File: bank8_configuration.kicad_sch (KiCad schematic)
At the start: 19 parts, among them IC1 ECP5-BGA256, U7 W25Q32JVSS

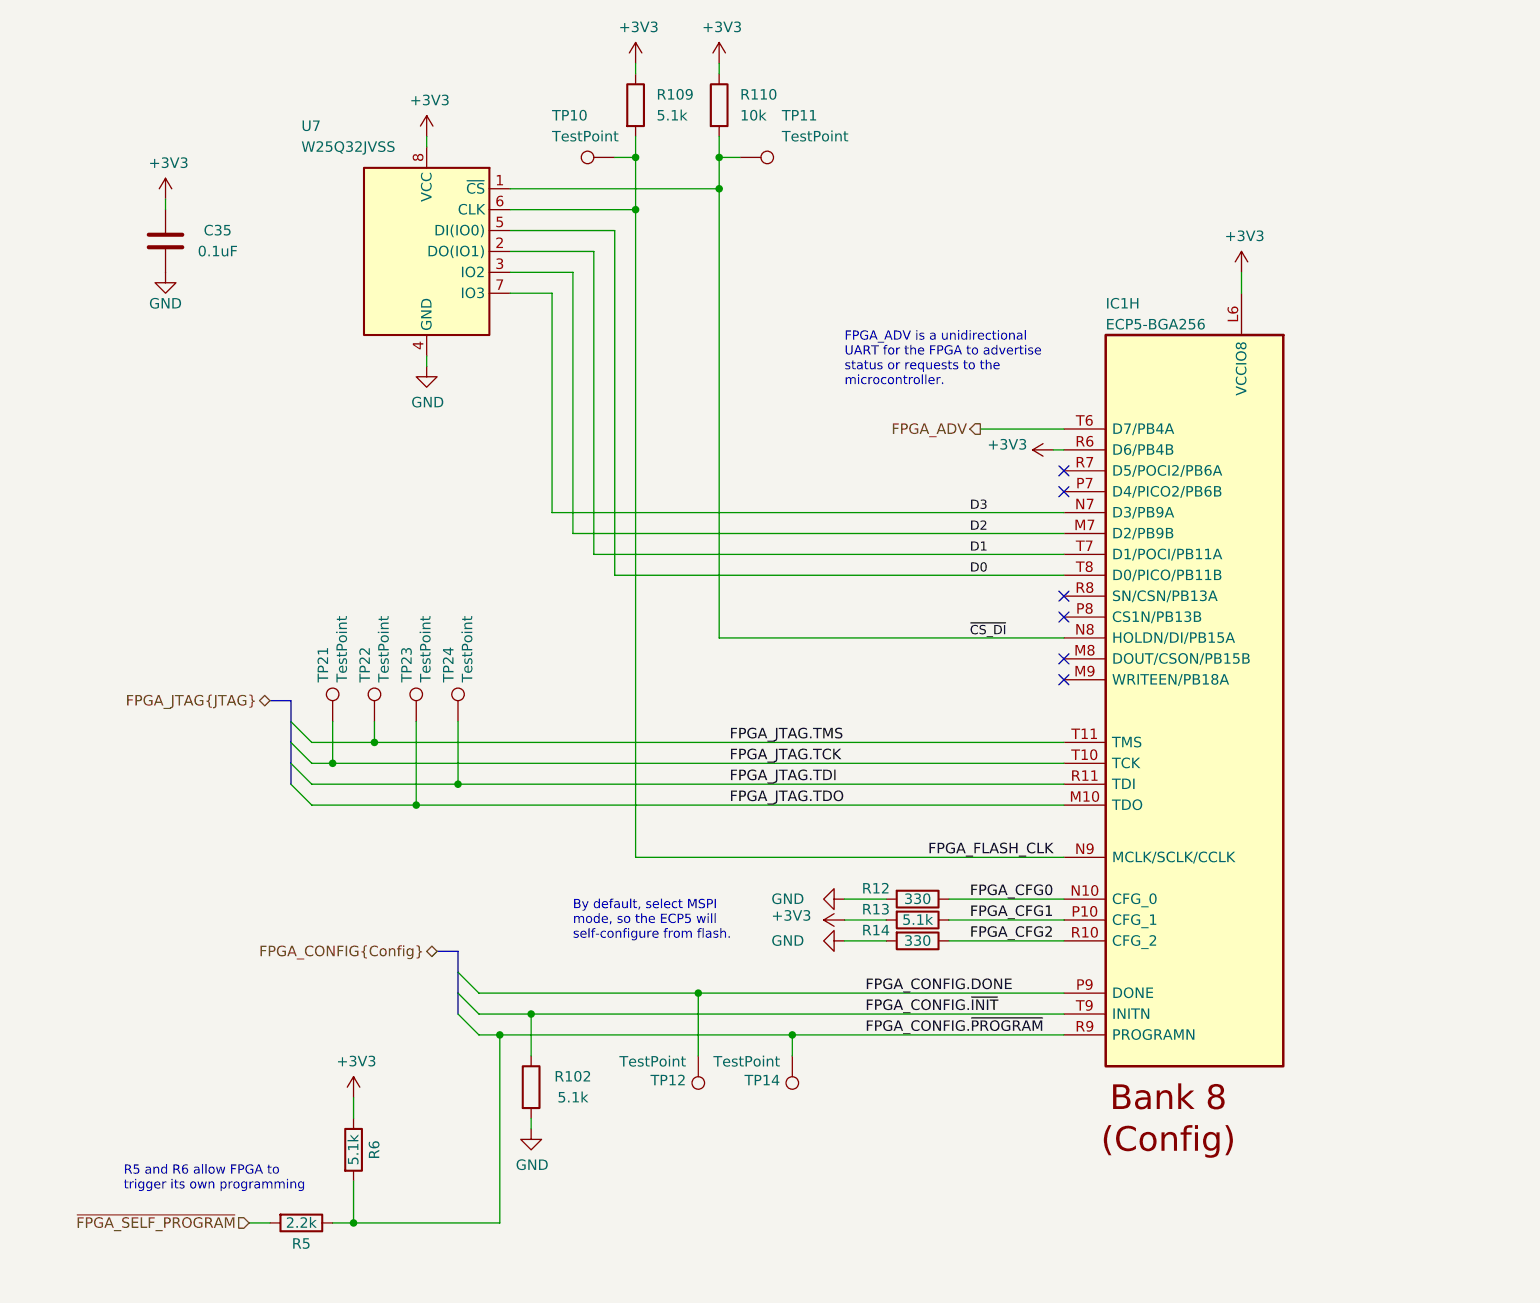
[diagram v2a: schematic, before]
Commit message: Clean up schematic
- Renumber Pmod signal names to match silkscreen labels
- Clean up FPGA symbol
- Clean up PHY symbol
- Add title block to newer sheets
- Fix horizontal line in LED sheet
- Improve various label positions
- Update data sheet fields
- Renumber pages
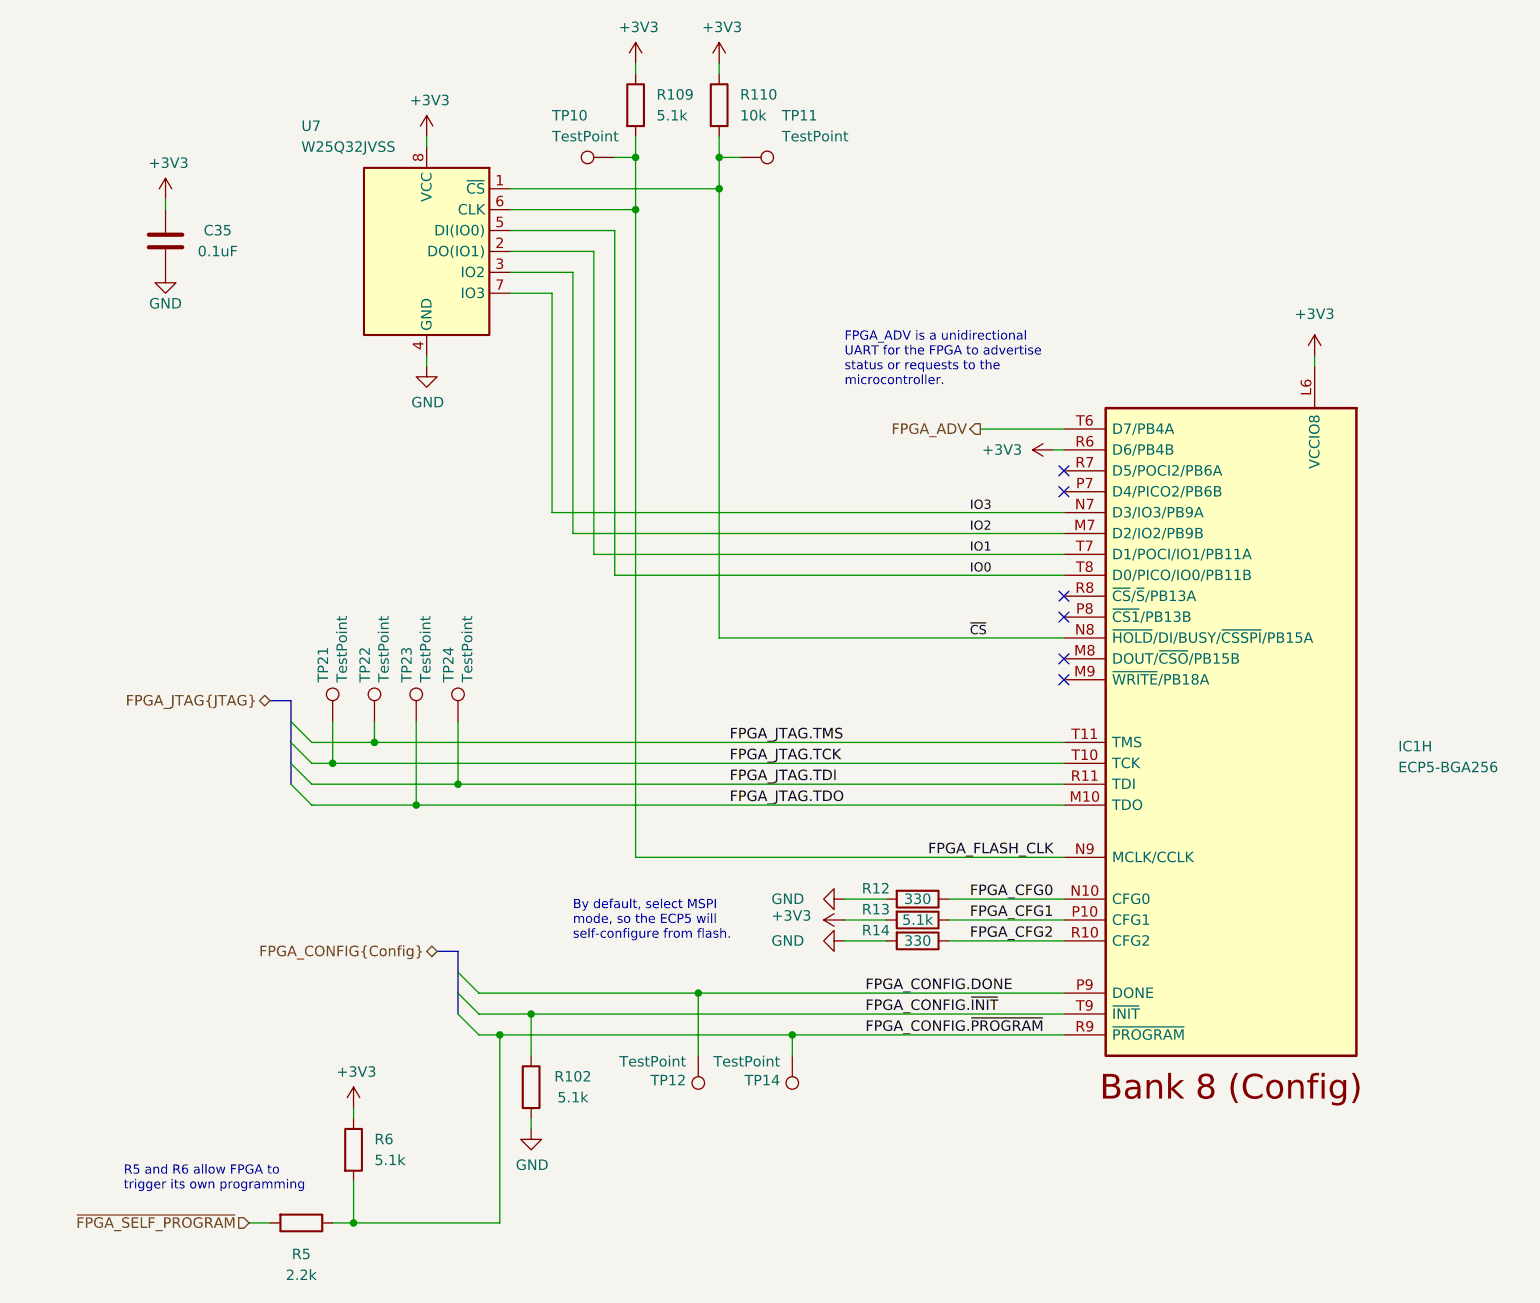
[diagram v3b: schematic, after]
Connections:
- net D0 renamed IO0
- net D1 renamed IO1
- net D2 renamed IO2
- net D3 renamed IO3
- net ~{CS_DI} renamed ~{CS}
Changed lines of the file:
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@@
     (stroke (width 0) (type default))
   )
-  (wire (pts (xy 198.12 50.8) (xy 198.12 48.26))
+  (wire (pts (xy 207.01 59.69) (xy 207.01 58.42))
     (stroke (width 0) (type default))
   )
@@
     (stroke (width 0) (type default))
   )
-  (wire (pts (xy 90.17 148.59) (xy 90.17 151.13))
+  (wire (pts (xy 90.17 149.86) (xy 90.17 151.13))
     (stroke (width 0) (type default))
   )
@@
     (effects (font (size 1.27 1.27)) (justify left bottom))
   )
-  (label "D1" (at 165.1 82.55 0) (fields_autoplaced)
+  (label "IO1" (at 165.1 82.55 0) (fields_autoplaced)
     (effects (font (size 1.1176 1.1176)) (justify left bottom))
   )
@@
     (effects (font (size 1.27 1.27)) (justify left bottom))
   )
-  (label "D0" (at 165.1 85.09 0) (fields_autoplaced)
+  (label "IO0" (at 165.1 85.09 0) (fields_autoplaced)
     (effects (font (size 1.1176 1.1176)) (justify left bottom))
   )
-  (label "D3" (at 165.1 77.47 0) (fields_autoplaced)
+  (label "IO3" (at 165.1 77.47 0) (fields_autoplaced)
     (effects (font (size 1.1176 1.1176)) (justify left bottom))
   )
-  (label "D2" (at 165.1 80.01 0) (fields_autoplaced)
+  (label "IO2" (at 165.1 80.01 0) (fields_autoplaced)
     (effects (font (size 1.1176 1.1176)) (justify left bottom))
   )
@@
     (effects (font (size 1.27 1.27)) (justify left bottom))
   )
-  (label "~{CS_DI}" (at 165.1 92.71 0) (fields_autoplaced)
+  (label "~{CS}" (at 165.1 92.71 0) (fields_autoplaced)
     (effects (font (size 1.1176 1.1176)) (justify left bottom))
   )
@@
     (effects (font (size 1.27 1.27)) (justify right))
   )
-  (symbol (lib_id "fpgas_and_processors:ECP5-BGA256") (at 203.2 55.88 0) (mirror y) (unit 8)
-    (in_bom yes) (on_board yes) (dnp no)
-    (property "Reference" "IC1" (at 181.61 52.07 0)
+  (symbol (lib_id "fpgas_and_processors:ECP5-BGA256") (at 196.85 104.14 0) (mirror y) (unit 8)
+    (in_bom yes) (on_board yes) (dnp no) (fields_autoplaced)
+    (property "Reference" "IC1" (at 217.17 105.9043 0)
       (effects (font (size 1.27 1.27)) (justify right))
     )
-    (property "Value" "ECP5-BGA256" (at 181.61 54.61 0)
+    (property "Value" "ECP5-BGA256" (at 217.17 108.4443 0)
       (effects (font (size 1.27 1.27)) (justify right))
     )
-    (property "Footprint" "cynthion:lattice_cabga256" (at 284.48 -31.75 0)
+    (property "Footprint" "cynthion:lattice_cabga256" (at 278.13 16.51 0)
       (effects (font (size 1.27 1.27)) (justify left) hide)
     )
-    (property "Datasheet" "" (at 295.91 -55.88 0)
+    (property "Datasheet" "https://www.latticesemi.com/-/media/LatticeSemi/Documents/DataSheets/ECP5/FPGA-DS-02012-2-2-ECP5-ECP5G-Family-Data-Sheet.ashx?document_id=50461" (at 289.56 -7.62 0)
       (effects (font (size 1.27 1.27)) (justify left) hide)
     )
-    (property "Description" "FPGA - Field Programmable Gate Array ECP5; 12k LUTs; 1.1V" (at 295.91 -53.34 0)
+    (property "Description" "FPGA - Field Programmable Gate Array ECP5; 12k LUTs; 1.1V" (at 289.56 -5.08 0)
       (effects (font (size 1.27 1.27)) (justify left) hide)
     )
-    (property "Manufacturer" "Lattice" (at 294.64 -77.47 0)
+    (property "Manufacturer" "Lattice" (at 288.29 -29.21 0)
       (effects (font (size 1.27 1.27)) (justify left) hide)
     )
-    (property "Part Number" "LFE5U-12F-6BG256C" (at 294.64 -74.93 0)
+    (property "Part Number" "LFE5U-12F-6BG256C" (at 288.29 -26.67 0)
       (effects (font (size 1.27 1.27)) (justify left) hide)
     )
-    (property "Substitution" "LFE5U-12F-*BG256*, LFE5U-25F-*BG256*" (at 203.2 55.88 0)
+    (property "Substitution" "LFE5U-12F-*BG256*, LFE5U-25F-*BG256*" (at 196.85 104.14 0)
       (effects (font (size 1.27 1.27)) hide)
     )
@@
     )
   )
-  (symbol (lib_id "power:+3V3") (at 198.12 48.26 0) (unit 1)
-    (in_bom yes) (on_board yes) (dnp no)
-    (property "Reference" "#PWR056" (at 198.12 52.07 0)
-      (effects (font (size 1.27 1.27)) hide)
-    )
-    (property "Value" "+3V3" (at 198.501 43.8658 0)
-      (effects (font (size 1.27 1.27)))
-    )
-    (property "Footprint" "" (at 198.12 48.26 0)
-      (effects (font (size 1.27 1.27)) hide)
-    )
-    (property "Datasheet" "" (at 198.12 48.26 0)
+  (symbol (lib_id "power:+3V3") (at 207.01 58.42 0) (unit 1)
+    (in_bom yes) (on_board yes) (dnp no) (fields_autoplaced)
+    (property "Reference" "#PWR056" (at 207.01 62.23 0)
+      (effects (font (size 1.27 1.27)) hide)
+    )
+    (property "Value" "+3V3" (at 207.01 53.34 0)
+      (effects (font (size 1.27 1.27)))
+    )
+    (property "Footprint" "" (at 207.01 58.42 0)
+      (effects (font (size 1.27 1.27)) hide)
+    )
+    (property "Datasheet" "" (at 207.01 58.42 0)
       (effects (font (size 1.27 1.27)) hide)
     )
@@
     )
   )
-  (symbol (lib_id "power:+3V3") (at 90.17 148.59 0) (unit 1)
-    (in_bom yes) (on_board yes) (dnp no)
-    (property "Reference" "#PWR02" (at 90.17 152.4 0)
-      (effects (font (size 1.27 1.27)) hide)
-    )
-    (property "Value" "+3V3" (at 90.5256 144.1958 0)
-      (effects (font (size 1.27 1.27)))
-    )
-    (property "Footprint" "" (at 90.17 148.59 0)
-      (effects (font (size 1.27 1.27)) hide)
-    )
-    (property "Datasheet" "" (at 90.17 148.59 0)
+  (symbol (lib_id "power:+3V3") (at 90.17 149.86 0) (unit 1)
+    (in_bom yes) (on_board yes) (dnp no)
+    (property "Reference" "#PWR02" (at 90.17 153.67 0)
+      (effects (font (size 1.27 1.27)) hide)
+    )
+    (property "Value" "+3V3" (at 90.5256 145.4658 0)
+      (effects (font (size 1.27 1.27)))
+    )
+    (property "Footprint" "" (at 90.17 149.86 0)
+      (effects (font (size 1.27 1.27)) hide)
+    )
+    (property "Datasheet" "" (at 90.17 149.86 0)
       (effects (font (size 1.27 1.27)) hide)
     )
@@
   )
   (symbol (lib_id "Device:R") (at 90.17 154.94 0) (unit 1)
-    (in_bom yes) (on_board yes) (dnp no)
-    (property "Reference" "R6" (at 92.71 154.94 90)
-      (effects (font (size 1.27 1.27)))
-    )
-    (property "Value" "5.1k" (at 90.17 154.94 90)
-      (effects (font (size 1.27 1.27)))
+    (in_bom yes) (on_board yes) (dnp no) (fields_autoplaced)
+    (property "Reference" "R6" (at 92.71 153.67 0)
+      (effects (font (size 1.27 1.27)) (justify left))
+    )
+    (property "Value" "5.1k" (at 92.71 156.21 0)
+      (effects (font (size 1.27 1.27)) (justify left))
     )
     (property "Footprint" "Resistor_SMD:R_0402_1005Metric" (at 88.392 154.94 90)
@@
   )
   (symbol (lib_id "Device:R") (at 83.82 163.83 270) (unit 1)
-    (in_bom yes) (on_board yes) (dnp no)
-    (property "Reference" "R5" (at 83.82 166.37 90)
-      (effects (font (size 1.27 1.27)))
-    )
-    (property "Value" "2.2k" (at 83.82 163.83 90)
+    (in_bom yes) (on_board yes) (dnp no) (fields_autoplaced)
+    (property "Reference" "R5" (at 83.82 167.64 90)
+      (effects (font (size 1.27 1.27)))
+    )
+    (property "Value" "2.2k" (at 83.82 170.18 90)
       (effects (font (size 1.27 1.27)))
     )
@@
   )
   (symbol (lib_id "power:+3V3") (at 175.26 69.85 90) (unit 1)
-    (in_bom yes) (on_board yes) (dnp no)
+    (in_bom yes) (on_board yes) (dnp no) (fields_autoplaced)
     (property "Reference" "#PWR0206" (at 179.07 69.85 0)
       (effects (font (size 1.27 1.27)) hide)
     )
-    (property "Value" "+3V3" (at 172.085 69.215 90)
-      (effects (font (size 1.27 1.27)) (justify left))
-    )
+    (property "Value" "+3V3" (at 171.45 69.85 90)
+      (effects (font (size 1.27 1.27)) (justify left))
+    )

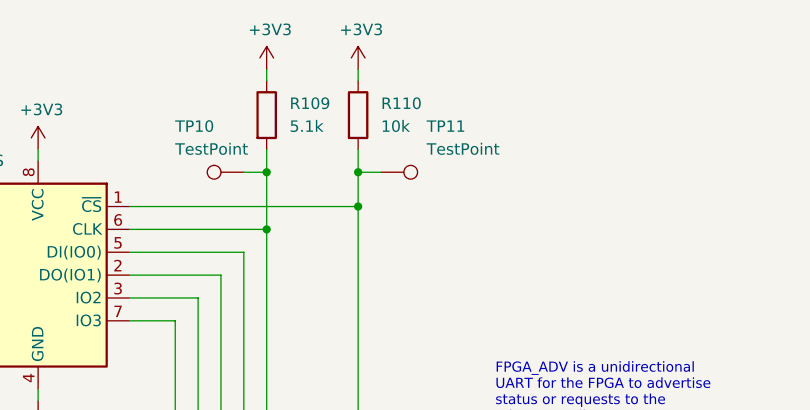
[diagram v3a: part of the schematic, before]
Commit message: Change R110 chip select pull-up from 10k to 5.1k
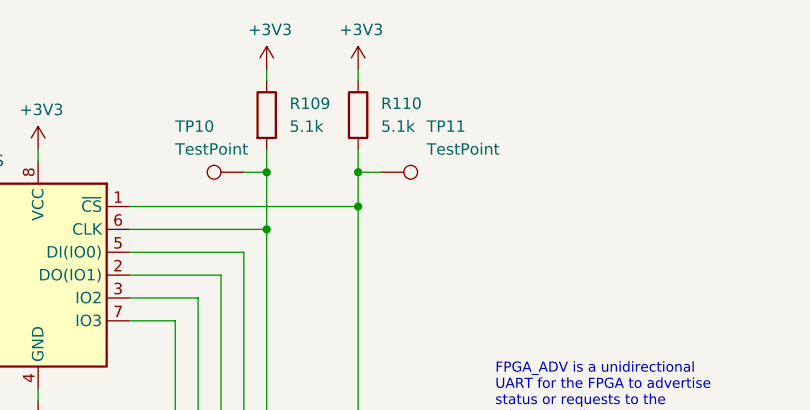
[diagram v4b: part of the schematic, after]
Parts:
- R102: Substitution 5.1k -> any equivalent
- R110: value 10k -> 5.1k; Part Number RC0402JR-0710KL -> RC0402JR-075K1L
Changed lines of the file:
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@@
       (effects (font (size 1.27 1.27)) hide)
     )
-    (property "Substitution" "5.1k" (at 111.76 147.32 0)
+    (property "Substitution" "any equivalent" (at 111.76 147.32 0)
       (effects (font (size 1.27 1.27)) hide)
     )
@@
       (effects (font (size 1.27 1.27)) (justify left))
     )
-    (property "Value" "10k" (at 137.16 29.21 0)
+    (property "Value" "5.1k" (at 137.16 29.21 0)
       (effects (font (size 1.27 1.27)) (justify left))
     )
@@
       (effects (font (size 1.27 1.27)) hide)
     )
-    (property "Part Number" "RC0402JR-0710KL" (at 134.62 27.94 0)
+    (property "Part Number" "RC0402JR-075K1L" (at 134.62 27.94 0)
       (effects (font (size 1.27 1.27)) hide)
     )
@@
       (effects (font (size 1.27 1.27)) hide)
     )
-    (property "Description" "RES 10K OHM 5% 1/16W 0402" (at 134.62 27.94 0)
+    (property "Description" "RES 5.1K OHM 5% 1/16W 0402" (at 134.62 27.94 0)
       (effects (font (size 1.27 1.27)) hide)
     )

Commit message: Update copyright notices
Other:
- company: Copyright 2019-2023 Great Scott Gadgets -> ${COPYRIGHT}
- title: Cynthion -> ${TITLE}
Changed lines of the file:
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@@
   (paper "A4")
   (title_block
-    (title "Cynthion")
+    (title "${TITLE}")
     (date "${DATE}")
     (rev "${VERSION}")
-    (company "Copyright 2019-2023 Great Scott Gadgets")
-    (comment 1 "Licensed under the CERN-OHL-P v2")
+    (company "${COPYRIGHT}")
+    (comment 1 "${LICENSE}")
   )
   (bus_alias "Config" (members "DONE" "~{INIT}" "~{PROGRAM}"))
